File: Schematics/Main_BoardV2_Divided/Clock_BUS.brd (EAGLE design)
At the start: 157.5 x 148.3 mm, 87 parts

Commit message: Routd and Cams Created
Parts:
- moved 16BBUS1:13 55.9 mm to (19.1, 16.5)
- moved 16BBUS1:14 55.9 mm to (19.1, 41.9)
- moved 16BBUS1:7 55.9 mm to (80.0, 41.9)
- moved 16BBUS1:8 55.9 mm to (80.0, 16.5)
- moved 16BBUS1:IC10 55.9 mm to (19.1, 29.2)
- moved 16BBUS1:IC7 55.9 mm to (80.0, 29.2)
- moved 16BBUS1:1 55.9 mm to (52.1, 21.6)
- moved 16BBUS1:11 55.9 mm to (31.8, 31.8)
- moved 16BBUS1:12 55.9 mm to (31.8, 21.6)
- moved 16BBUS1:15 55.9 mm to (11.4, 31.8)
- moved 16BBUS1:16 55.9 mm to (11.4, 21.6)
- moved 16BBUS1:2 55.9 mm to (52.1, 31.8)
- moved 16BBUS1:3 55.9 mm to (59.7, 41.9)
- moved 16BBUS1:4 55.9 mm to (72.4, 21.6)
- moved 16BBUS1:5 55.9 mm to (59.7, 16.5)
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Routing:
- net VCC: track 0.00 -> 177.4 mm
- net N$59: track 0.00 -> 148.5 mm, vias 0 -> 1
- net N$61: track 0.00 -> 143.9 mm
- net N$55: track 0.00 -> 138.1 mm, vias 0 -> 1
- net N$58: track 0.00 -> 137.6 mm
- net N$60: track 0.00 -> 134.8 mm
- net N$57: track 0.00 -> 125.4 mm, vias 0 -> 1
- net N$54: track 0.00 -> 121.4 mm
- net N$56: track 0.00 -> 119.6 mm
- net N$50: track 0.00 -> 117.6 mm
- net N$53: track 0.00 -> 109.4 mm
- net N$51: track 0.00 -> 105.3 mm
- net N$52: track 0.00 -> 104.7 mm
- net N$38: track 0.00 -> 95.9 mm
- net N$49: track 0.00 -> 93.6 mm
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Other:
- board size 157.5 x 148.3 mm -> 157.5 x 145.7 mm
- board text added: "A/M Switch"
- board text added: "Clock Speed"
- board text added: "Manual Pulse"

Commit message: Visual Improvments
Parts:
- CLK1:R7: device pot:3RP/1610N -> 555:POT
- CLK1:S2: device switch:320-916 -> 4-1825136-5:TE_4-1825136-5
- SV1, SV10, SV2, SV3, SV4, SV5, SV6, SV7, SV8, SV9: device con-lstb:MA08-1 -> pinhead:1X08
- SV11, SV12, SV13, SV14: device con-lstb:MA08-2 -> pinhead:2X08
- X1: device con-wago-500:W237-102 -> pinhead:1X02
- turned CLK1:S2 to 0 degrees
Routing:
- net VCC: track 177.4 -> 178.7 mm
- net CLK1:N$1: track 27.5 -> 28.2 mm

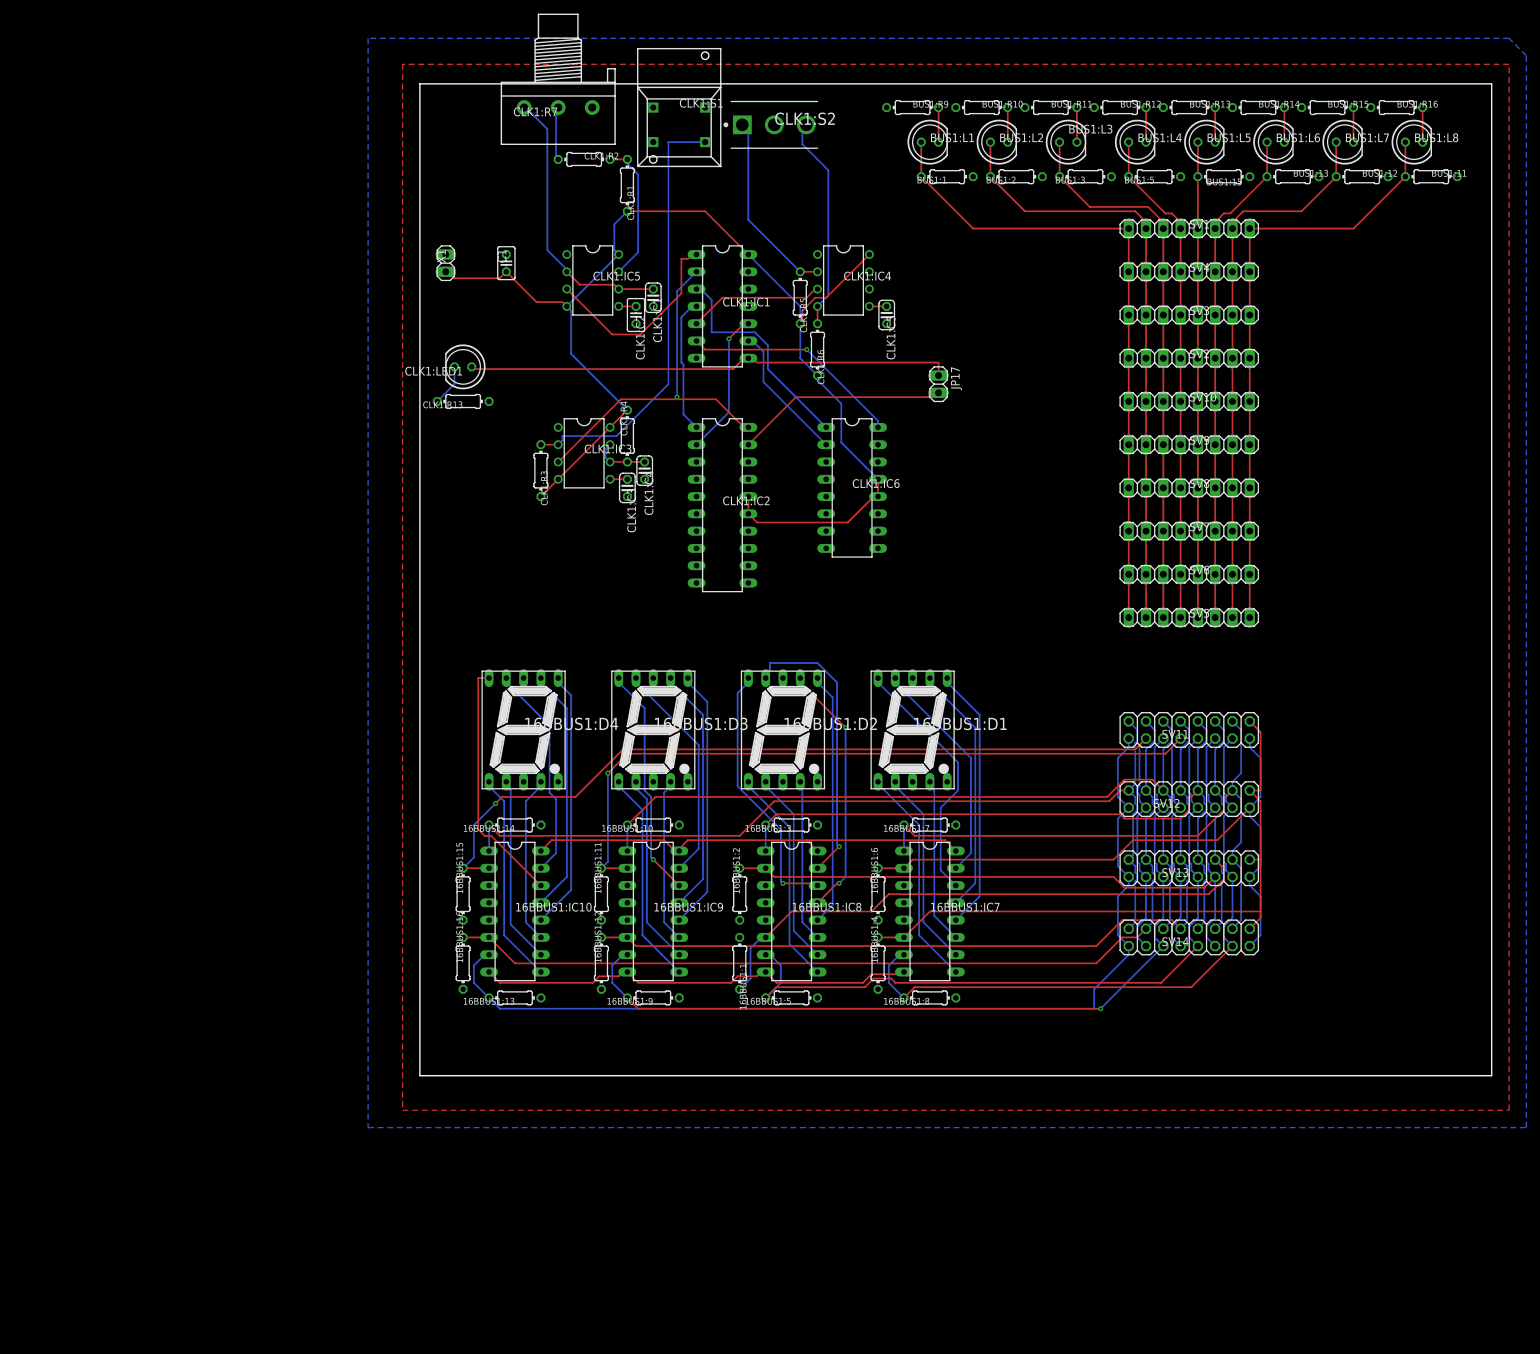
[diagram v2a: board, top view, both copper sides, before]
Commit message: Microcode Added and Ram Updated
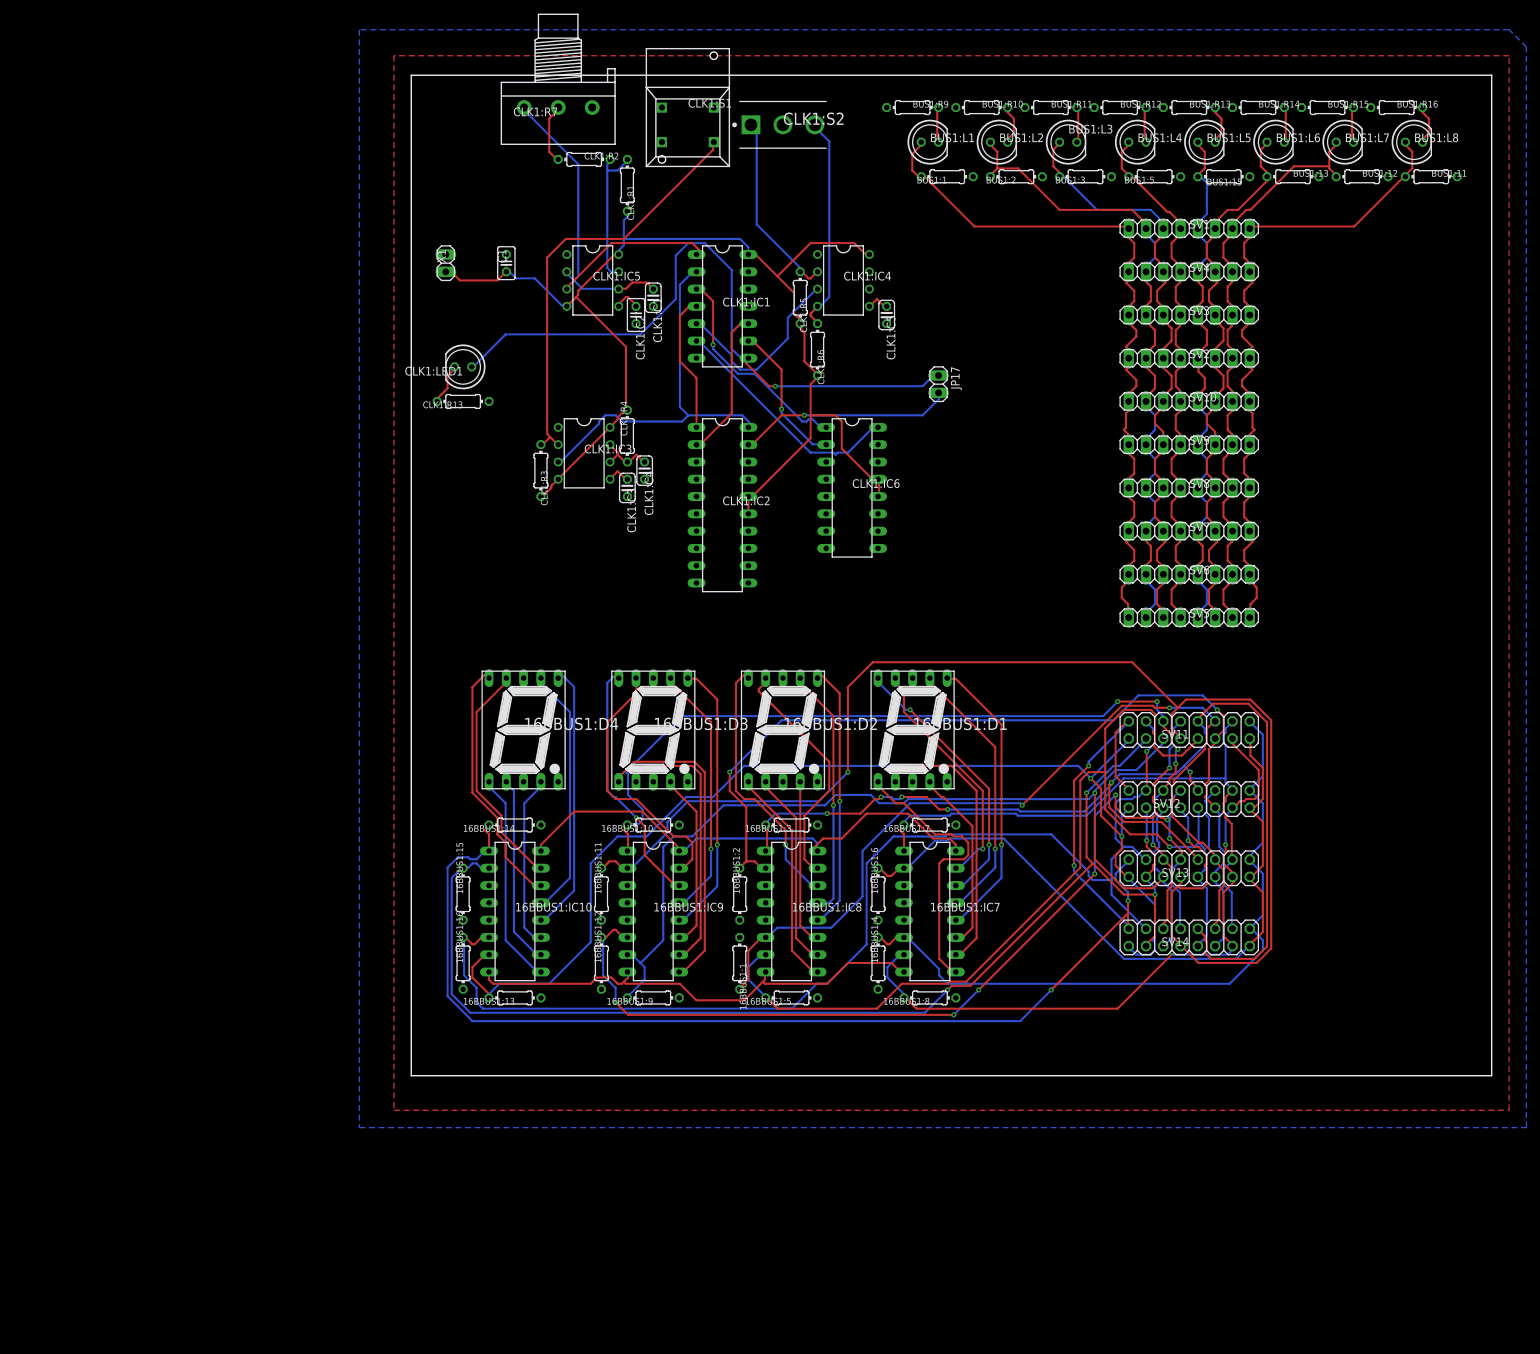
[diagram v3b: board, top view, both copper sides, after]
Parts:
- moved CLK1:S1 1.27 mm to (44.5, 147.3)
- moved CLK1:S2 1.27 mm to (58.4, 144.8)
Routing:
- net N$55: track 138.1 -> 208.4 mm, vias 1 -> 2
- net N$60: track 134.8 -> 200.1 mm, vias 0 -> 4
- net N$52: track 104.7 -> 165.1 mm, vias 0 -> 6
- net N$53: track 109.4 -> 154.5 mm, vias 0 -> 1
- net N$54: track 121.4 -> 158.3 mm, vias 0 -> 8
- net N$59: track 148.5 -> 185.2 mm, vias 1 -> 4
- net N$58: track 137.6 -> 171.9 mm, vias 0 -> 1
- net N$51: track 105.3 -> 135.7 mm, vias 0 -> 2
- net N$57: track 125.4 -> 154.6 mm
- net N$50: track 117.6 -> 144.5 mm, vias 0 -> 2
- net CLK: track 71.5 -> 97.0 mm, vias 0 -> 1
- net N$61: track 143.9 -> 167.3 mm, vias 0 -> 2
- net N$56: track 119.6 -> 135.6 mm, vias 0 -> 5
- net 16BBUS1:N$35: track 31.6 -> 46.2 mm
- net 16BBUS1:N$34: track 28.0 -> 39.6 mm
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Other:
- board size 157.5 x 145.7 mm -> 158.7 x 147 mm
